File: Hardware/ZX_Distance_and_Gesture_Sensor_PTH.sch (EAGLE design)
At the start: 50 parts, among them Q1 MMBT2222A, Q2 MOSFET-NCHANNEL2N7002PW, U1 PIC16F1823-14PINTSSOP, U2 MCP6291T-E/OT, U3 DMC2700UDM, U4 DMC2700UDM, U5 BRM-2508VERT, U6 TSOP57238TT1

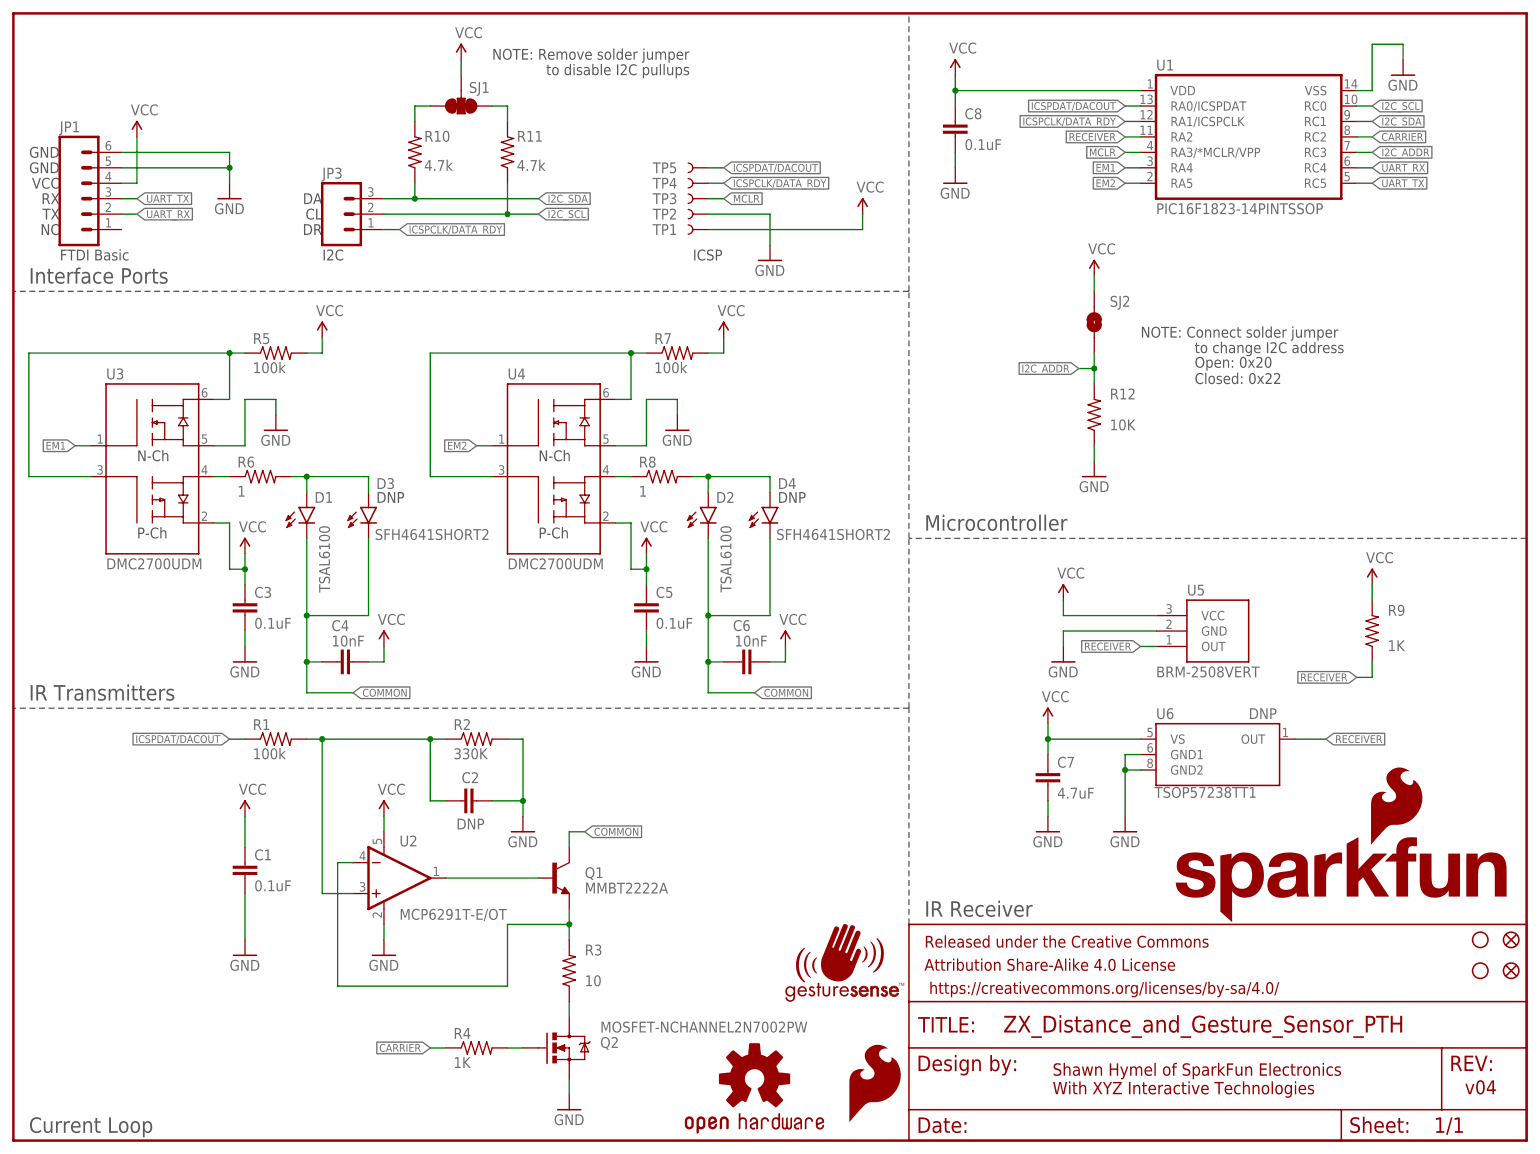
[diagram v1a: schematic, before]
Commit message: Updated U2, U5, R2. Changed to v05.
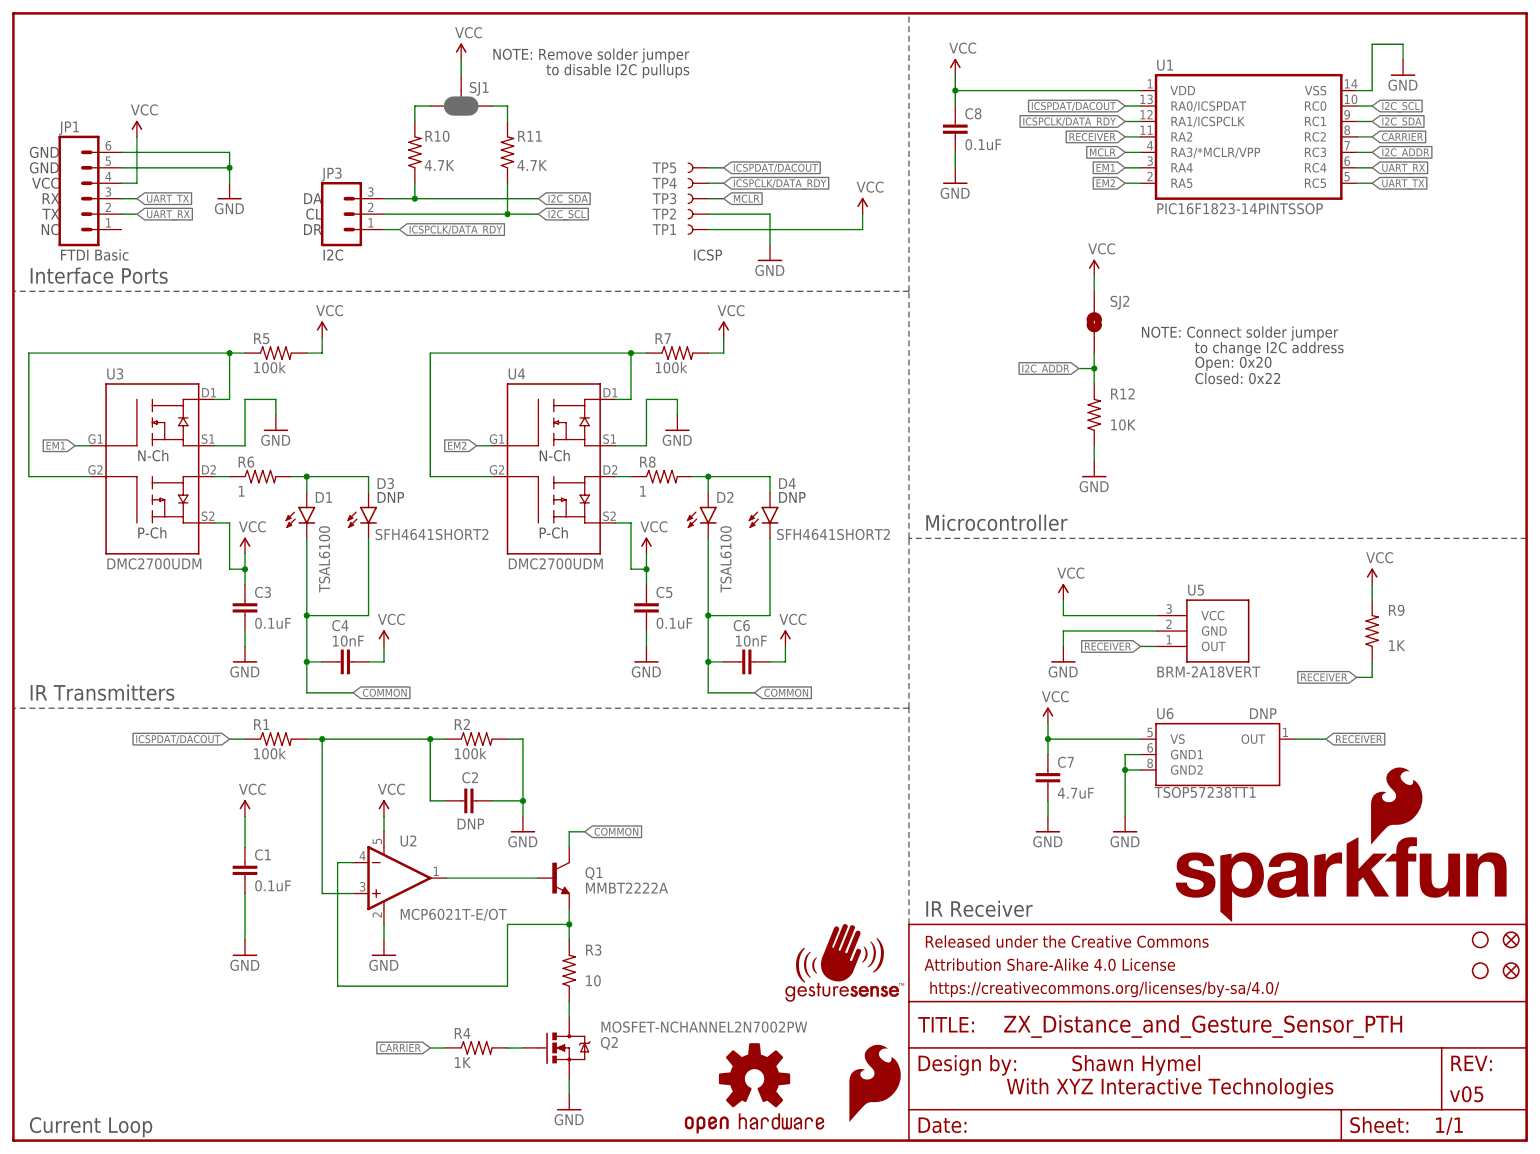
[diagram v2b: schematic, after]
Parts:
- FRAME1: value FRAME-LETTER -> (none); DESIGNER (none) -> Shawn Hymel; VERSION (none) -> v05
- JP1: device SparkFun-Connectors:M06NO_SILK -> SparkFun-Connectors:M06NO_SILK_FEMALE_PTH
- R1, R5, R7: device SparkFun-Resistors:100KOHM1/10W1%(0603) -> SparkFun-Resistors:100KOHM-1/10W-1%(0603)
- R10, R11: value 4.7k -> 4.7K; device SparkFun-Resistors:4.7KOHM1/10W1%(0603) -> SparkFun-Resistors:4.7KOHM-1/10W-1%(0603)
- R12: device SparkFun-Resistors:10KOHM1/10W1%(0603)0603 -> SparkFun-Resistors:10KOHM-1/10W-1%(0603)0603
- R2: value 330K -> 100k; device SparkFun-Resistors:330KOHM1/10W1%(0603)0603 -> SparkFun-Resistors:100KOHM-1/10W-1%(0603)
- R3: device SparkFun-Resistors:10OHM1/10W5%0603SMD -> SparkFun-Resistors:10OHM-1/10W-5%0603SMD
- R4, R9: device SparkFun-Resistors:1KOHM1/10W1%(0603) -> SparkFun-Resistors:1KOHM-1/10W-1%(0603)
- SJ1: value (none) -> JUMPER-PAD-3-NC_BY_PASTE; device SparkFun-Passives:SOLDERJUMPER_2WAYPASTE1&2&3 -> SparkFun-Passives:JUMPER-PAD-3-NC_BY_PASTE
- SJ2: value SOLDERJUMPERNO -> JUMPER-PAD-2-NOYES_SILK; device SparkFun-Passives:SOLDERJUMPERNO -> SparkFun-Passives:JUMPER-PAD-2-NOYES_SILK
- U2: value MCP6291T-E/OT -> MCP6021T-E/OT; device SparkFun-AnalogIC:MCP6291T-E/OT -> SparkFun-AnalogIC:MCP6021T-E/OT
- U5: value BRM-2508VERT -> BRM-2A18VERT; device SparkFun-Sensors:BRM-2508VERT -> SparkFun-Sensors:BRM-2A18VERT
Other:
- note added: "With XYZ Interactive Technologies"
- note removed: "Shawn Hymel of SparkFun Electronics With XYZ Interactive Technologies"
- note removed: "v04"
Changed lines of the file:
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@@
 <?xml version="1.0" encoding="utf-8"?>
 <!DOCTYPE eagle SYSTEM "eagle.dtd">
-<eagle version="6.5.0">
+<eagle version="7.2.0">
 <drawing>
 <settings>
@@
 <setting verticaltext="up"/>
 </settings>
-<grid distance="0.1" unitdist="inch" unit="inch" style="lines" multiple="1" display="yes" altdistance="0.01" altunitdist="inch" altunit="inch"/>
+<grid distance="0.1" unitdist="inch" unit="inch" style="lines" multiple="1" display="no" altdistance="0.01" altunitdist="inch" altunit="inch"/>
 <layers>
 <layer number="1" name="Top" color="4" fill="1" visible="no" active="no"/>
@@
 <layer number="56" name="wert" color="7" fill="1" visible="no" active="no"/>
 <layer number="57" name="tCAD" color="7" fill="1" visible="no" active="no"/>
+<layer number="90" name="Modules" color="5" fill="1" visible="yes" active="yes"/>
 <layer number="91" name="Nets" color="2" fill="1" visible="yes" active="yes"/>
 <layer number="92" name="Busses" color="1" fill="1" visible="yes" active="yes"/>
@@
 <layer number="251" name="SMDround" color="12" fill="11" visible="no" active="no"/>
 <layer number="254" name="cooling" color="7" fill="1" visible="yes" active="yes"/>
+<layer number="255" name="routoute" color="7" fill="1" visible="yes" active="yes"/>
 </layers>
 <schematic xreflabel="%F%N/%S.%C%R" xrefpart="/%S.%C%R">
@@
 </classes>
 <parts>
-<part name="FRAME1" library="SparkFun-Aesthetics" deviceset="FRAME-LETTER" device=""/>
+<part name="FRAME1" library="SparkFun-Aesthetics" deviceset="FRAME-LETTER" device="">
+<attribute name="DESIGNER" value="Shawn Hymel"/>
+<attribute name="VERSION" value="v05"/>
+</part>
 <part name="U1" library="SparkFun-DigitalIC" deviceset="PIC16F1823-14PIN" device="TSSOP"/>
-<part name="U2" library="SparkFun-AnalogIC" deviceset="MCP6291" device="T-E/OT"/>
+<part name="U2" library="SparkFun-AnalogIC" deviceset="MCP6021" device="T-E/OT"/>
 <part name="Q1" library="SparkFun-DiscreteSemi" deviceset="TRANSISTOR_NPN" device="MMBT2222A" value="MMBT2222A"/>
 <part name="Q2" library="SparkFun-DiscreteSemi" deviceset="MOSFET-NCHANNEL" device="2N7002PW"/>
@@
 <attribute name="PLACE" value="DNP"/>
 </part>
-<part name="JP1" library="SparkFun-Connectors" deviceset="M06" device="NO_SILK"/>
+<part name="JP1" library="SparkFun-Connectors" deviceset="M06" device="NO_SILK_FEMALE_PTH"/>
 <part name="JP3" library="SparkFun-Connectors" deviceset="M03" device="1X03_NO_SILK"/>
 <part name="GND1" library="SparkFun-Aesthetics" deviceset="GND" device=""/>
@@
 <part name="SUPPLY2" library="SparkFun-Aesthetics" deviceset="VCC" device=""/>
 <part name="GND2" library="SparkFun-Aesthetics" deviceset="GND" device=""/>
-<part name="R1" library="SparkFun-Resistors" deviceset="100KOHM1/10W1%(0603)" device="" value="100k"/>
-<part name="R2" library="SparkFun-Resistors" deviceset="330KOHM1/10W1%(0603)" device="0603" value="330K"/>
-<part name="R3" library="SparkFun-Resistors" deviceset="10OHM1/10W5%0603" device="SMD" value="10"/>
-<part name="R4" library="SparkFun-Resistors" deviceset="1KOHM1/10W1%(0603)" device="" value="1K"/>
+<part name="R1" library="SparkFun-Resistors" deviceset="100KOHM-1/10W-1%(0603)" device="" value="100k"/>
+<part name="R2" library="SparkFun-Resistors" deviceset="100KOHM-1/10W-1%(0603)" device="" value="100k"/>
+<part name="R3" library="SparkFun-Resistors" deviceset="10OHM-1/10W-5%0603" device="SMD" value="10"/>
+<part name="R4" library="SparkFun-Resistors" deviceset="1KOHM-1/10W-1%(0603)" device="" value="1K"/>
 <part name="C1" library="SparkFun-Capacitors" deviceset="0.1UF-25V(+80/-20%)(0603)" device="" value="0.1uF"/>
 <part name="C2" library="SparkFun-Capacitors" deviceset="CAP" device="0603-CAP" value="DNP"/>
@@
 <attribute name="VARIANT" value="TSAL6100"/>
 </part>
-<part name="R5" library="SparkFun-Resistors" deviceset="100KOHM1/10W1%(0603)" device="" value="100k"/>
+<part name="R5" library="SparkFun-Resistors" deviceset="100KOHM-1/10W-1%(0603)" device="" value="100k"/>
 <part name="R6" library="SparkFun-Resistors" deviceset="1OHM1/10W1%(0603)" device="" value="1"/>
 <part name="C3" library="SparkFun-Capacitors" deviceset="0.1UF-25V(+80/-20%)(0603)" device="" value="0.1uF"/>
@@
 <part name="GND8" library="SparkFun-Aesthetics" deviceset="GND" device=""/>
 <part name="SUPPLY7" library="SparkFun-Aesthetics" deviceset="VCC" device=""/>
-<part name="R7" library="SparkFun-Resistors" deviceset="100KOHM1/10W1%(0603)" device="" value="100k"/>
+<part name="R7" library="SparkFun-Resistors" deviceset="100KOHM-1/10W-1%(0603)" device="" value="100k"/>
 <part name="SUPPLY8" library="SparkFun-Aesthetics" deviceset="VCC" device=""/>
 <part name="GND9" library="SparkFun-Aesthetics" deviceset="GND" device=""/>
@@
 <part name="SUPPLY10" library="SparkFun-Aesthetics" deviceset="VCC" device=""/>
 <part name="GND10" library="SparkFun-Aesthetics" deviceset="GND" device=""/>
-<part name="R9" library="SparkFun-Resistors" deviceset="1KOHM1/10W1%(0603)" device="" value="1K"/>
+<part name="R9" library="SparkFun-Resistors" deviceset="1KOHM-1/10W-1%(0603)" device="" value="1K"/>
 <part name="C7" library="SparkFun-Capacitors" deviceset="4.7UF-6.3V-10%(0603)" device="0603" value="4.7uF"/>
 <part name="GND11" library="SparkFun-Aesthetics" deviceset="GND" device=""/>
@@
 <part name="SUPPLY14" library="SparkFun-Aesthetics" deviceset="VCC" device=""/>
 <part name="GND14" library="SparkFun-Aesthetics" deviceset="GND" device=""/>
-<part name="R10" library="SparkFun-Resistors" deviceset="4.7KOHM1/10W1%(0603)" device="" value="4.7k"/>
-<part name="R11" library="SparkFun-Resistors" deviceset="4.7KOHM1/10W1%(0603)" device="" value="4.7k"/>
-<part name="SJ1" library="SparkFun-Passives" deviceset="SOLDERJUMPER_2WAY" device="PASTE1&amp;2&amp;3"/>
+<part name="R10" library="SparkFun-Resistors" deviceset="4.7KOHM-1/10W-1%(0603)" device="" value="4.7K"/>
+<part name="R11" library="SparkFun-Resistors" deviceset="4.7KOHM-1/10W-1%(0603)" device="" value="4.7K"/>
+<part name="SJ1" library="SparkFun-Passives" deviceset="JUMPER-PAD-3-NC_BY_PASTE" device=""/>
 <part name="SUPPLY13" library="SparkFun-Aesthetics" deviceset="VCC" device=""/>
-<part name="R12" library="SparkFun-Resistors" deviceset="10KOHM1/10W1%(0603)" device="0603" value="10K"/>
+<part name="R12" library="SparkFun-Resistors" deviceset="10KOHM-1/10W-1%(0603)" device="0603" value="10K"/>
 <part name="GND15" library="SparkFun-Aesthetics" deviceset="GND" device=""/>
-<part name="SJ2" library="SparkFun-Passives" deviceset="SOLDERJUMPER" device="NO"/>
+<part name="SJ2" library="SparkFun-Passives" deviceset="JUMPER-PAD-2-NO" device="YES_SILK"/>
 <part name="SUPPLY15" library="SparkFun-Aesthetics" deviceset="VCC" device=""/>
 <part name="FID1" library="SparkFun-Aesthetics" deviceset="FIDUCIAL" device="1X2"/>
@@
 <part name="TP4" library="SparkFun-Passives" deviceset="TEST-POINT" device="3X4" value="TEST-POINT3X4"/>
 <part name="TP5" library="SparkFun-Passives" deviceset="TEST-POINT" device="3X4" value="TEST-POINT3X4"/>
-<part name="U5" library="SparkFun-Sensors" deviceset="BRM-2508" device="VERT"/>
+<part name="U5" library="SparkFun-Sensors" deviceset="BRM-2A18" device="VERT"/>
 <part name="SUPPLY16" library="SparkFun-Aesthetics" deviceset="VCC" device=""/>
 <part name="GND16" library="SparkFun-Aesthetics" deviceset="GND" device=""/>
@@
 <sheet>
 <plain>
-<text x="238.76" y="7.62" size="2.286" layer="94">v04</text>
-<text x="170.942" y="7.62" size="2.032" layer="94">Shawn Hymel of SparkFun Electronics
-With XYZ Interactive Technologies</text>
+<text x="163.322" y="7.62" size="2.54" layer="94">With XYZ Interactive Technologies</text>
 <text x="7.62" y="144.78" size="1.778" layer="97">FTDI Basic</text>
 <text x="50.8" y="144.78" size="1.778" layer="97">I2C</text>
@@
 <instances>
 <instance part="FRAME1" gate="G$1" x="0" y="0"/>
-<instance part="FRAME1" gate="G$2" x="147.32" y="0"/>
+<instance part="FRAME1" gate="V" x="147.32" y="0"/>
 <instance part="U1" gate="G$1" x="203.2" y="165.1" smashed="yes">
 <attribute name="NAME" x="187.96" y="176.022" size="1.778" layer="95"/>
@@
 <instance part="SJ1" gate="G$1" x="73.66" y="170.18" smashed="yes" rot="R270">
 <attribute name="NAME" x="74.93" y="172.339" size="1.778" layer="95"/>
-<attribute name="VALUE" x="71.755" y="167.64" size="1.778" layer="96" rot="R270"/>
 </instance>
 <instance part="SUPPLY13" gate="G$1" x="73.66" y="177.8"/>
@@
 </instance>
 <instance part="GND15" gate="1" x="177.8" y="109.22"/>
-<instance part="SJ2" gate="1" x="177.8" y="134.62" smashed="yes" rot="R90">
+<instance part="SJ2" gate="G$1" x="177.8" y="134.62" smashed="yes" rot="R90">
 <attribute name="NAME" x="180.34" y="137.16" size="1.778" layer="95"/>
 <attribute name="VALUE" x="180.34" y="137.16" size="1.778" layer="96" display="off"/>
@@
 <segment>
 <pinref part="SUPPLY15" gate="G$1" pin="VCC"/>
-<pinref part="SJ2" gate="1" pin="2"/>
+<pinref part="SJ2" gate="G$1" pin="2"/>
 <wire x1="177.8" y1="142.24" x2="177.8" y2="139.7" width="0.1524" layer="91"/>
 </segment>
@@
 <net name="I2C_ADDR" class="0">
 <segment>
-<pinref part="SJ2" gate="1" pin="1"/>
+<pinref part="SJ2" gate="G$1" pin="1"/>
 <pinref part="R12" gate="G$1" pin="2"/>
 <wire x1="177.8" y1="124.46" x2="177.8" y2="127" width="0.1524" layer="91"/>

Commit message: Changed version number. Moved 1 trace. Removed ground pour under part.
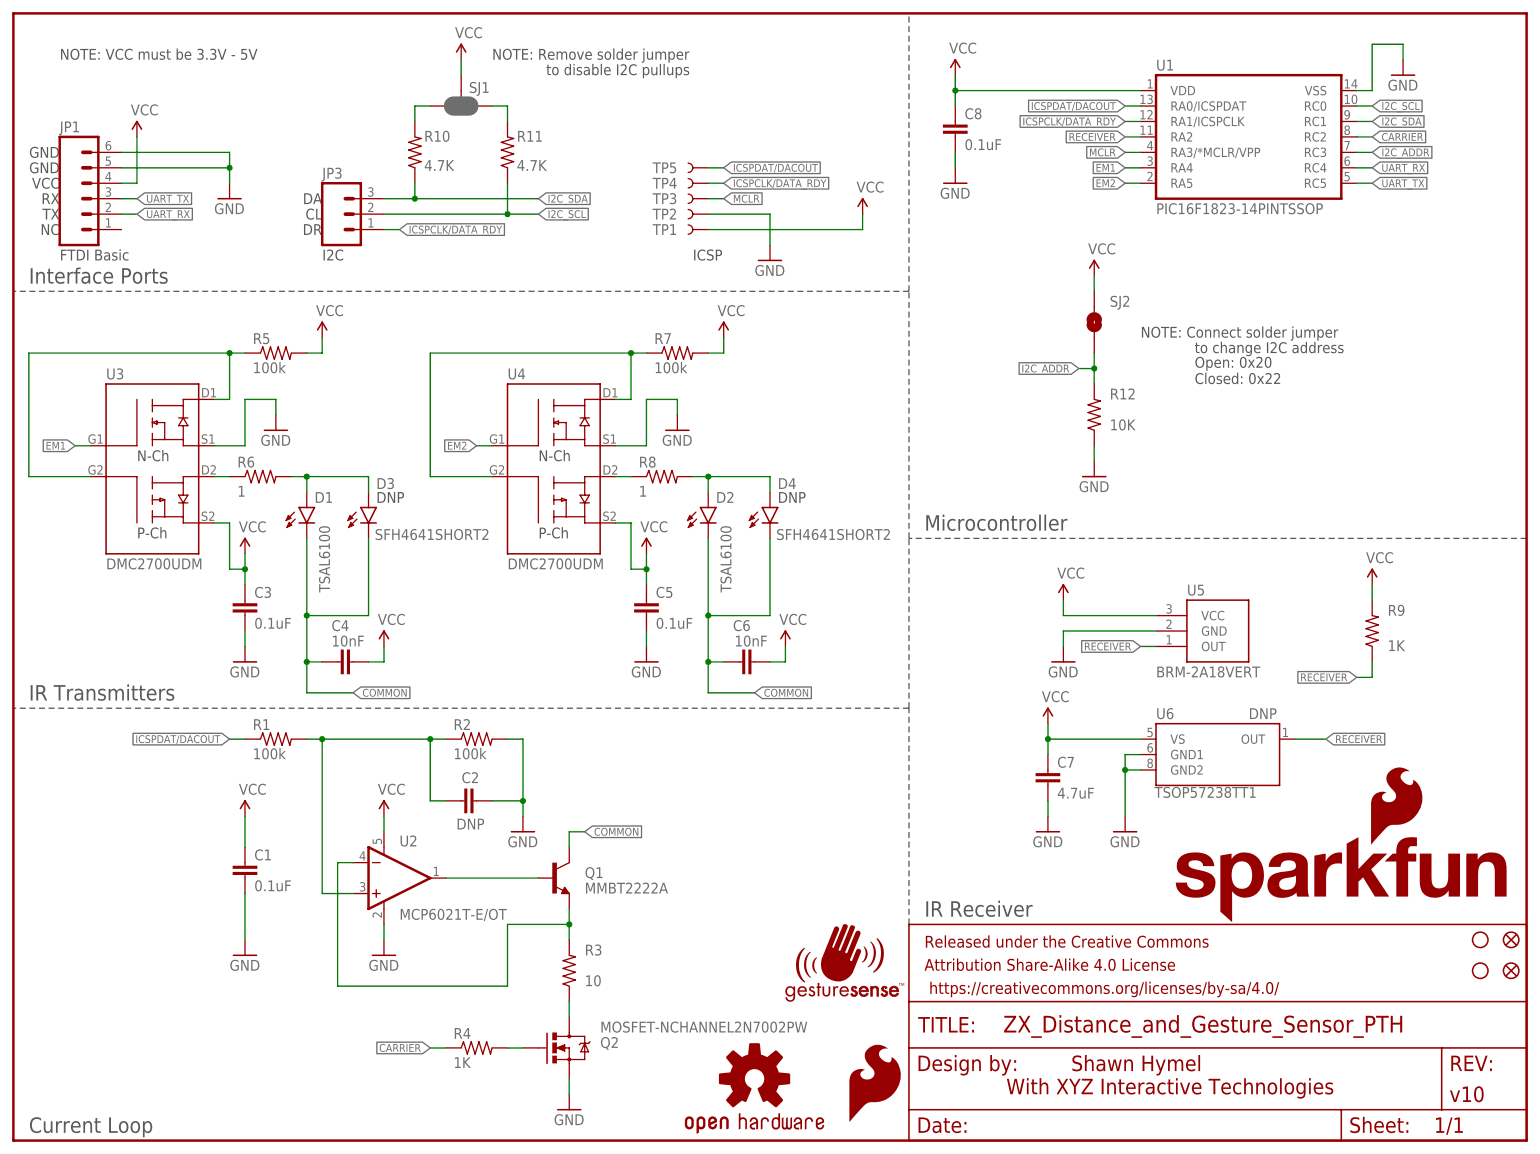
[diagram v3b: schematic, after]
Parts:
- FRAME1: VERSION v05 -> v10
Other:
- note added: "NOTE: VCC must be 3.3V - 5V"
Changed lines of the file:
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@@
 <part name="FRAME1" library="SparkFun-Aesthetics" deviceset="FRAME-LETTER" device="">
 <attribute name="DESIGNER" value="Shawn Hymel"/>
-<attribute name="VERSION" value="v05"/>
+<attribute name="VERSION" value="v10"/>
 </part>
 <part name="U1" library="SparkFun-DigitalIC" deviceset="PIC16F1823-14PIN" device="TSSOP"/>
@@
 <text x="59.69" y="104.902" size="1.778" layer="97">DNP</text>
 <text x="125.73" y="104.902" size="1.778" layer="97">DNP</text>
+<text x="7.62" y="177.8" size="1.778" layer="97">NOTE: VCC must be 3.3V - 5V</text>
 </plain>
 <instances>
